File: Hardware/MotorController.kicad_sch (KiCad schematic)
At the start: 9 parts, among them U3 STSPIN250

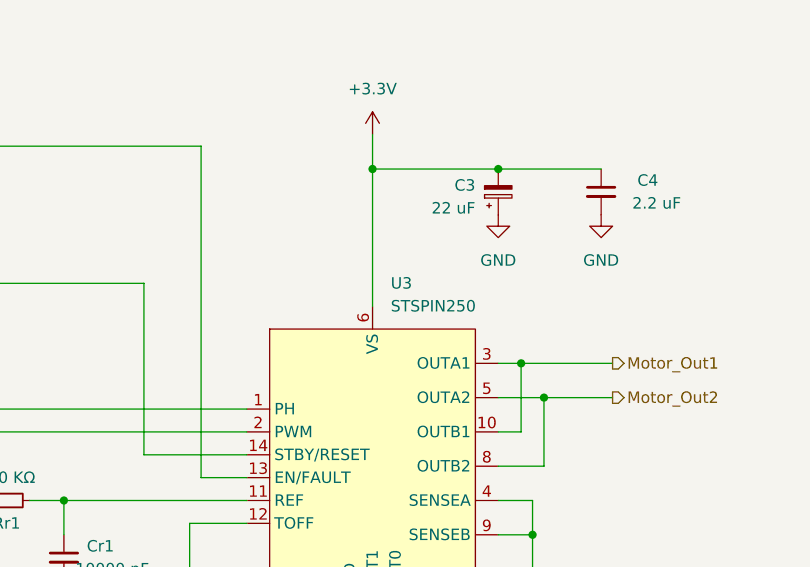
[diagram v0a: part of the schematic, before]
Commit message: Fix Thoughholes
Fixed Schematic Parity DRC issue.

Taught some standard practices by the Foxy Boy

Co-Authored-By: KenwoodFox <31870999+KenwoodFox@users.noreply.github.com>
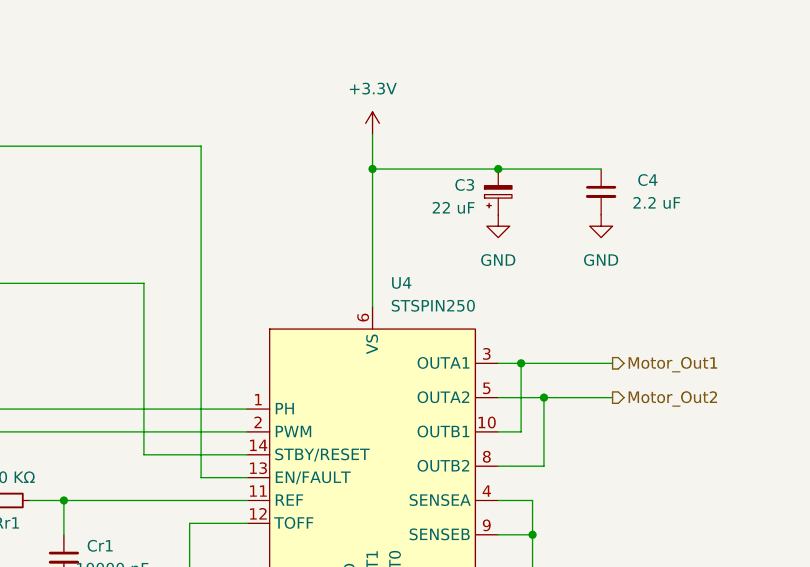
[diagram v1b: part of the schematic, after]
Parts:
- renumbered U3 to U4
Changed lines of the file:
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@@
   (symbol (lib_id "power:+3.3V") (at 148.59 76.2 0) (mirror y) (unit 1)
     (in_bom yes) (on_board yes)
-    (property "Reference" "#PWR017" (id 0) (at 148.59 80.01 0)
+    (property "Reference" "#PWR023" (id 0) (at 148.59 80.01 0)
       (effects (font (size 1.27 1.27)) hide)
     )
@@
   (symbol (lib_id "power:GND") (at 162.56 85.09 0) (mirror y) (unit 1)
     (in_bom yes) (on_board yes) (fields_autoplaced)
-    (property "Reference" "#PWR019" (id 0) (at 162.56 91.44 0)
+    (property "Reference" "#PWR025" (id 0) (at 162.56 91.44 0)
       (effects (font (size 1.27 1.27)) hide)
     )
@@
   (symbol (lib_id "power:GND") (at 128.27 144.78 0) (unit 1)
     (in_bom yes) (on_board yes) (fields_autoplaced)
-    (property "Reference" "#PWR016" (id 0) (at 128.27 151.13 0)
+    (property "Reference" "#PWR022" (id 0) (at 128.27 151.13 0)
       (effects (font (size 1.27 1.27)) hide)
     )
@@
   (symbol (lib_id "Amoskeag-KiCAD-Lib:STSPIN250") (at 148.59 95.25 0) (unit 1)
     (in_bom yes) (on_board yes) (fields_autoplaced)
-    (property "Reference" "U3" (id 0) (at 150.6094 92.71 0)
+    (property "Reference" "U4" (id 0) (at 150.6094 92.71 0)
       (effects (font (size 1.27 1.27)) (justify left))
     )
@@
   (symbol (lib_id "power:GND") (at 114.3 124.46 0) (unit 1)
     (in_bom yes) (on_board yes) (fields_autoplaced)
-    (property "Reference" "#PWR015" (id 0) (at 114.3 130.81 0)
+    (property "Reference" "#PWR021" (id 0) (at 114.3 130.81 0)
       (effects (font (size 1.27 1.27)) hide)
     )
@@
   (symbol (lib_id "power:GND") (at 148.59 144.78 0) (unit 1)
     (in_bom yes) (on_board yes) (fields_autoplaced)
-    (property "Reference" "#PWR018" (id 0) (at 148.59 151.13 0)
+    (property "Reference" "#PWR024" (id 0) (at 148.59 151.13 0)
       (effects (font (size 1.27 1.27)) hide)
     )
@@
   (symbol (lib_id "power:GND") (at 166.37 144.78 0) (unit 1)
     (in_bom yes) (on_board yes) (fields_autoplaced)
-    (property "Reference" "#PWR020" (id 0) (at 166.37 151.13 0)
+    (property "Reference" "#PWR026" (id 0) (at 166.37 151.13 0)
       (effects (font (size 1.27 1.27)) hide)
     )
@@
   (symbol (lib_id "power:GND") (at 173.99 85.09 0) (mirror y) (unit 1)
     (in_bom yes) (on_board yes) (fields_autoplaced)
-    (property "Reference" "#PWR021" (id 0) (at 173.99 91.44 0)
-      (effects (font (size 1.27 1.27)) hide)
-    )
+    (property "Reference" "#PWR027" (id 0) (at 173.99 91.44 0)
+      (effects (font (size 1.27 1.27)) hide)
+    )

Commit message: Add Throughholes
Added Through holes in a far better what than before.

Got advice from the Foxy Fellow

Co-Authored-By: KenwoodFox <31870999+KenwoodFox@users.noreply.github.com>
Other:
- title: STSPIN250 Module -> TurtleBot Mainboard
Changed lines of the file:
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@@
   (paper "A4")
   (title_block
-    (title "STSPIN250 Module")
-    (date "2022-11-26")
-    (rev "0.1")
+    (title "TurtleBot Mainboard")
+    (date "2022-11-27")
+    (rev "${REVISION}")
     (company "Amoskeag Technologies")
+    (comment 4 "${FULL_REVISION}")
   )
   (junction (at 165.1 101.6) (diameter 0) (color 0 0 0 0)
